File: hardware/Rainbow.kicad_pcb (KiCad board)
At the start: 2 copper layers, 53.2 x 38.7 mm, 26 parts, among them J1 PICKit3, J2 UART, J3 JUMPER, J4 JACK, J5 RGB, J6 RGB, J7 RGB, J8 RGB, Q1 Q_NMOS_GDS, Q2 Q_NMOS_GDS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

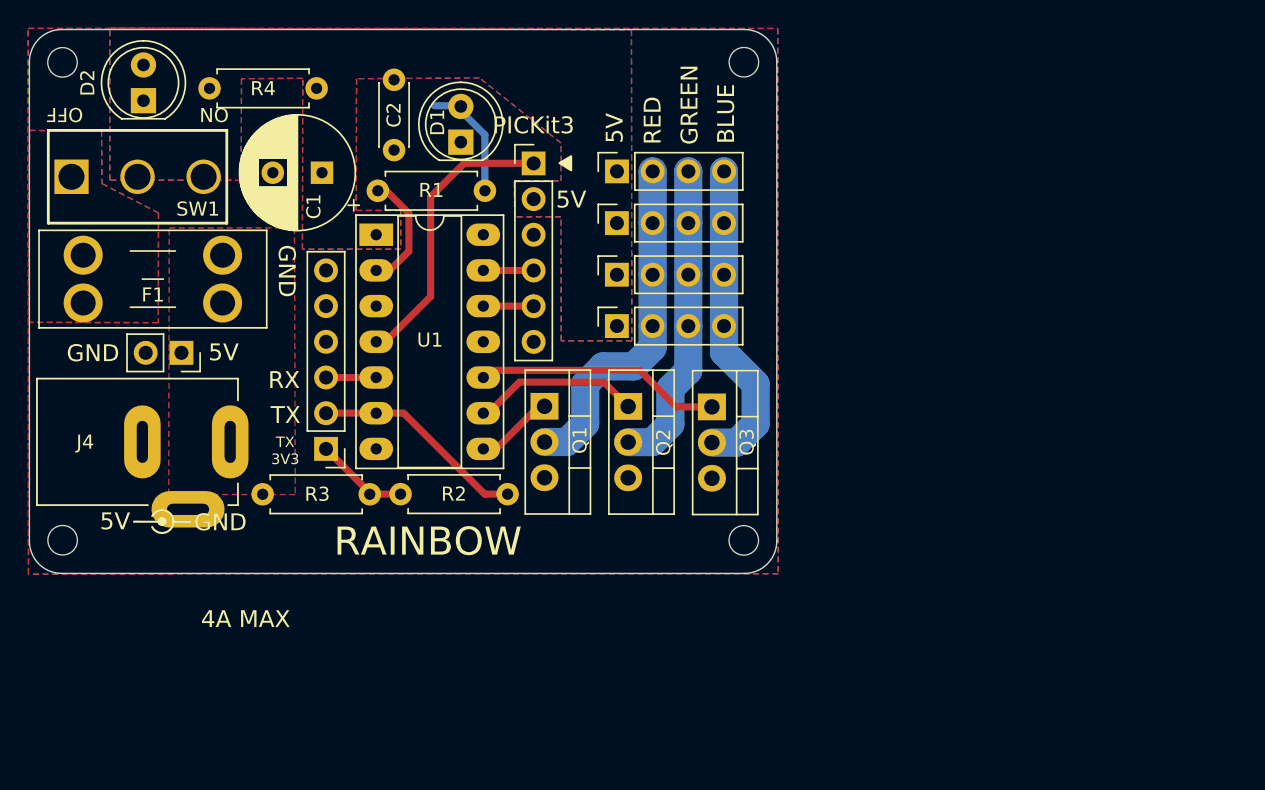
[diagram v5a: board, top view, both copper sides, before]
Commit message: Re-engineer board for flexible power supply
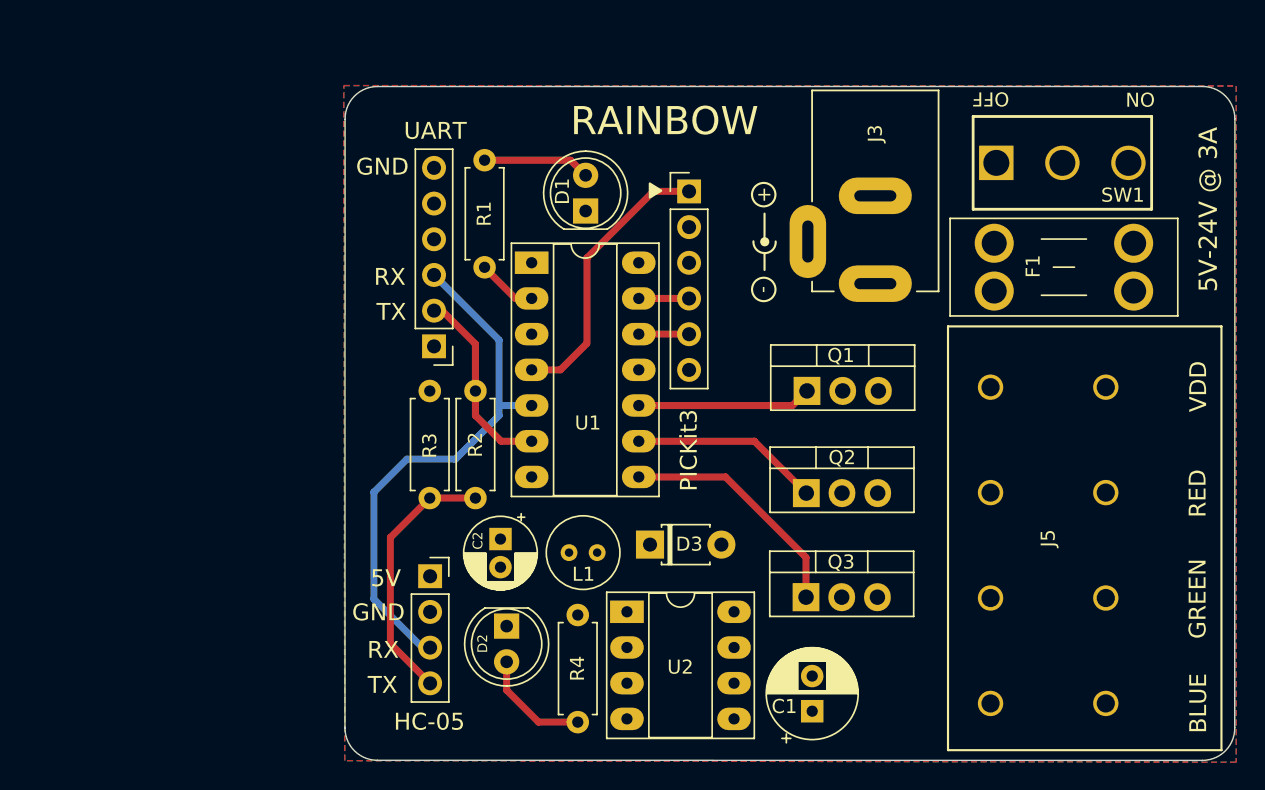
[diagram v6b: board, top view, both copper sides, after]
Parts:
- removed H1, H2, H3, H4: MountingHole, MountingHole:MountingHole_2.1mm
- removed J6, J7, J8: RGB, Connector_PinSocket_2.54mm:PinSocket_1x04_P2.54mm_Vertical
- added D3: D_Schottky, Diode_THT:D_T-1_P5.08mm_Horizontal, F.Cu at (133.6, 96.0)
- added L1: 100uH, Capacitor_THT:C_Radial_D5.0mm_H7.0mm_P2.00mm, F.Cu at (129.9, 96.5)
- added U2: MIC4574-5.0YN, Package_DIP:DIP-8_W7.62mm_Socket_LongPads, F.Cu at (132.0, 100.7)
- C1: value 470uF -> 47uF; footprint Capacitor_THT:CP_Radial_D8.0mm_P3.50mm -> Capacitor_THT:CP_Radial_D6.3mm_P2.50mm
- C2: value 0.1uF -> 220uF; footprint Capacitor_THT:C_Disc_D4.3mm_W1.9mm_P5.00mm -> Capacitor_THT:CP_Radial_D5.0mm_P2.00mm
- J3: value JUMPER -> BARREL_JACK; footprint Connector_PinSocket_2.54mm:PinSocket_1x02_P2.54mm_Vertical -> Rainbow:Barrel_Jack
- J4: value JACK -> HC-05; footprint Tensility_Barrel_Jack:Tensility_Barrel_Jack -> Connector_PinSocket_2.54mm:PinSocket_1x04_P2.54mm_Vertical
- J5: footprint Connector_PinSocket_2.54mm:PinSocket_1x04_P2.54mm_Vertical -> Rainbow:Wago
- moved SW1 65.8 mm to (163.0, 68.8)
- moved F1 55.1 mm to (158.1, 74.5), turned to 0 degrees
- moved J3 52.8 mm to (149.7, 63.6)
- moved C1 51.8 mm to (145.2, 107.8), turned to 90 degrees
- moved J5 46.3 mm to (157.9, 107.2)
- moved R4 45.7 mm to (128.5, 101.0), turned to -90 degrees
- moved D2 45.4 mm to (123.4, 101.8), turned to -90 degrees
- moved J4 29.6 mm to (118.0, 98.2)
- moved C2 28.7 mm to (123.0, 95.6), turned to -90 degrees
- moved Q1 18.7 mm to (144.8, 85.0), turned to 0 degrees
- moved Q3 15.1 mm to (144.7, 99.7), turned to 0 degrees
- moved Q2 14.1 mm to (144.8, 92.3), turned to 0 degrees
- moved J1 11.2 mm to (136.4, 70.8)
- moved U1 11.2 mm to (125.2, 75.9)
- moved J2 10.6 mm to (118.3, 81.8)
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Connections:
- C1 pad 1: +5V -> VDC
- J2 pad 1: Net-(J2-Pad1) -> unconnected-(J2-Pad1)
- J4 pad 1: Net-(F1-Pad1) -> +5V
- J4 pad 3: GNDREF -> RX
- J5 pad 1: +5V -> Net-(J5-Pad1)
- J5 pad 2: Net-(J5-Pad2) -> Net-(J5-Pad1)
- J5 pad 4: Net-(J5-Pad4) -> Net-(J5-Pad3)
- Q1 pad 2: Net-(J5-Pad2) -> Net-(J5-Pad5)
- Q3 pad 2: Net-(J5-Pad4) -> Net-(J5-Pad1)
- R2 pad 2: Net-(J2-Pad1) -> Net-(J4-Pad4)
- R3 pad 1: Net-(J2-Pad1) -> Net-(J4-Pad4)
- SW1 pad 2: +5V -> Net-(F1-Pad2)
- SW1 pad 3: +5V -> VDC
- U1 pad 10: BLUE -> RED
- U1 pad 8: RED -> BLUE
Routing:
- net RX: track 3.54 -> 37.9 mm
- net Net-(J5-Pad2): track 24.7 -> 0.00 mm
- net Net-(J5-Pad4): track 22.6 -> 0.00 mm
- net Net-(J5-Pad3): track 22.1 -> 0.00 mm
- net Net-(J4-Pad4): track 0.00 -> 18.8 mm
- net RED: track 4.29 -> 12.4 mm
- net Net-(D2-Pad2): track 0.00 -> 8.02 mm
- net Net-(J2-Pad1): track 6.58 -> 0.00 mm
- net LED: track 8.46 -> 4.26 mm
- net TX: track 15.3 -> 13.2 mm
- net GREEN: track 11.6 -> 13.4 mm
- net Net-(D1-Pad2): track 8.43 -> 7.64 mm
- removed copper zone on B.Cu, net +5V
- removed copper zone on F.Cu, net +5V
- removed copper zone on F.Cu, net Net-(F1-Pad1)
- removed copper zone on B.Cu, net Net-(F1-Pad2)
- removed copper zone on F.Cu, net Net-(F1-Pad2)
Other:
- board size 53.2 x 38.7 mm -> 63.3 x 47.9 mm
- board text added: "+"
- board text added: "-"
- board text added: "5V-24V @ 3A"
- board text added: "HC-05"
- board text added: "UART"
- board text added: "VDD"
- board text removed: "4A MAX"
- board text removed: "TX 3V3"

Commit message: Finish wiring
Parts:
- moved SW1 4.55 mm to (166.2, 72.0), turned to 0 degrees
- moved F1 2.61 mm to (156.7, 76.7), turned to 90 degrees
- moved C1 2.15 mm to (147.3, 108.2)
- moved Q1 0.26 mm to (144.8, 84.8)
- moved Q3 0.05 mm to (144.7, 99.7)
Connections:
- J5 pad 1: Net-(J5-Pad1) -> VDC
- J5 pad 2: Net-(J5-Pad1) -> VDC
- J5 pad 7: VDC -> Net-(J5-Pad7)
- J5 pad 8: VDC -> Net-(J5-Pad7)
- Q1 pad 2: Net-(J5-Pad5) -> Net-(J5-Pad7)
- Q2 pad 2: Net-(J5-Pad3) -> Net-(J5-Pad5)
- Q3 pad 2: Net-(J5-Pad1) -> Net-(J5-Pad3)
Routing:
- net +5V: track 0.00 -> 52.2 mm
- net Net-(D3-Pad1): track 0.00 -> 14.4 mm
- net VDC: vias 0 -> 4
- added copper zone on B.Cu, net Net-(F1-Pad1)
- added copper zone on F.Cu, net Net-(F1-Pad1)
- added copper zone on B.Cu, net Net-(F1-Pad2)
- added copper zone on F.Cu, net Net-(F1-Pad2)
- added copper zone on F.Cu, net Net-(J5-Pad3)
- added copper zone on F.Cu, net Net-(J5-Pad5)
- added copper zone on F.Cu, net Net-(J5-Pad7)
- added copper zone on B.Cu, net VDC
- added copper zone on F.Cu, net VDC
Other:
- board text added: "5V-24V DC 8A MAX"
- board text removed: "5V-24V @ 3A"

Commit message: Clean up some PCB stuff
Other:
- board text added: "5V-24V DC 6A MAX"
- board text removed: "5V-24V DC 8A MAX"
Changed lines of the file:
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@@
     (effects (font (size 1.2 1.2) (thickness 0.2)))
   )
-  (gr_text "5V-24V DC\n8A MAX" (at 138.44 66.6 180) (layer "F.SilkS")
+  (gr_text "5V-24V DC\n6A MAX" (at 138.44 66.6 180) (layer "F.SilkS")
     (effects (font (size 1.3 1.3) (thickness 0.2)))
   )
@@
   (segment (start 121.86 68.6) (end 127.975 68.6) (width 0.5) (layer "F.Cu") (net 2))
   (segment (start 127.975 68.6) (end 129.05 69.675) (width 0.5) (layer "F.Cu") (net 2))
-  (segment (start 129.14 75.55) (end 129.14 81.63) (width 0.5) (layer "F.Cu") (net 3))
-  (segment (start 136.41 70.82) (end 133.87 70.82) (width 0.5) (layer "F.Cu") (net 3))
   (segment (start 129.14 81.63) (end 127.255 83.515) (width 0.5) (layer "F.Cu") (net 3))
+  (segment (start 136.41 70.82) (end 134.23 70.82) (width 0.5) (layer "F.Cu") (net 3))
+  (segment (start 129.14 75.91) (end 129.14 81.63) (width 0.5) (layer "F.Cu") (net 3))
   (segment (start 127.255 83.515) (end 125.21 83.515) (width 0.5) (layer "F.Cu") (net 3))
-  (segment (start 133.87 70.82) (end 129.14 75.55) (width 0.5) (layer "F.Cu") (net 3))
+  (segment (start 134.23 70.82) (end 129.14 75.91) (width 0.5) (layer "F.Cu") (net 3))
+  (segment (start 127.87 100.34) (end 128.49 100.96) (width 1) (layer "F.Cu") (net 4))
   (segment (start 126.904888 95.554888) (end 127.87 96.52) (width 1) (layer "F.Cu") (net 4))
-  (segment (start 127.87 100.34) (end 128.49 100.96) (width 1) (layer "F.Cu") (net 4))
+  (segment (start 127.87 96.52) (end 127.87 100.34) (width 1) (layer "F.Cu") (net 4))
   (segment (start 122.99 95.554888) (end 126.904888 95.554888) (width 1) (layer "F.Cu") (net 4))
   (segment (start 128.49 100.96) (end 131.76 100.96) (width 1) (layer "F.Cu") (net 4))
-  (segment (start 127.87 96.52) (end 127.87 100.34) (width 1) (layer "F.Cu") (net 4))
   (segment (start 122.99 95.554888) (end 120.630112 95.554888) (width 1) (layer "F.Cu") (net 4))
   (segment (start 120.630112 95.554888) (end 117.985 98.2) (width 1) (layer "F.Cu") (net 4))
@@
   (segment (start 123.43 104.29) (end 123.43 106.31) (width 0.5) (layer "F.Cu") (net 21))
   (segment (start 130.44 95.95) (end 129.87 96.52) (width 1) (layer "F.Cu") (net 22))
-  (segment (start 135.72 100.37) (end 138.62 103.27) (width 1) (layer "F.Cu") (net 22))
-  (segment (start 133.63 95.95) (end 135.72 98.04) (width 1) (layer "F.Cu") (net 22))
   (segment (start 138.62 103.27) (end 139.61 103.27) (width 1) (layer "F.Cu") (net 22))
-  (segment (start 135.72 98.04) (end 135.72 100.37) (width 1) (layer "F.Cu") (net 22))
+  (segment (start 133.63 95.95) (end 135.86 98.18) (width 1) (layer "F.Cu") (net 22))
   (segment (start 133.63 95.95) (end 130.44 95.95) (width 1) (layer "F.Cu") (net 22))
+  (segment (start 135.86 100.51) (end 138.62 103.27) (width 1) (layer "F.Cu") (net 22))
+  (segment (start 135.86 98.18) (end 135.86 100.51) (width 1) (layer "F.Cu") (net 22))
   (segment (start 115.16 95.44) (end 115.16 102.995) (width 0.5) (layer "F.Cu") (net 24))
   (segment (start 117.96 92.64) (end 115.16 95.44) (width 0.5) (layer "F.Cu") (net 24))
